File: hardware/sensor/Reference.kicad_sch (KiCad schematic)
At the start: 3 parts

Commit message: commit to save work from misbehaving laptop
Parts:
- removed R4: R, symbol Device:R
- added C?: 10u, symbol Device:C
- added Q? (x2): BC847BDW1, Package_TO_SOT_SMD:SOT-363_SC-70-6, symbol Transistor_BJT:BC847BDW1
- added U?: LTC2064, Package_SO:MSOP-8_3x3mm_P0.65mm, symbol sensorModules:LTC2064IMS8
- C13: value C -> 100n
- R3: value R -> 10k
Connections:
- net GND: now also C?.2, Q?.4 (E2)
- net V_{Ref}: now also U?.1, U?.2 (-); no longer C13.1, R3.2
- new net: Q?.1 (E1), Q?.3 (C2), Q?.5 (B2)
- new net: C13.1, C?.1, Q?.2 (B1), Q?.6 (C1), R3.2, U?.3 (+)
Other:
- moved on the sheet: C13, R3

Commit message: Fix incorrect upstream
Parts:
- removed Q? (x2): BC847BDW1, Package_TO_SOT_SMD:SOT-363_SC-70-6, symbol Transistor_BJT:BC847BDW1
- removed R3: 10k, symbol Device:R
- added J302: U_{ref}, testpoint_519x:Testpoint_519xTR, symbol Connector:Conn_01x01_Pin
- added J502: GND, testpoint_519x:Testpoint_519xTR, symbol Connector:Conn_01x01_Pin
- added R301, R302: R, Resistor_SMD:R_0805_2012Metric_Pad1.20x1.40mm_HandSolder, symbol Device:R
- C301: renamed from C13; footprint (none) -> Capacitor_SMD:C_0805_2012Metric_Pad1.18x1.45mm_HandSolder
- C302: renamed from C?; footprint (none) -> Capacitor_SMD:C_0805_2012Metric_Pad1.18x1.45mm_HandSolder
- gave numbers to parts that had none: 1
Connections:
- net GND: now also J502.1 (Pin_1), R302.2
- net V_{DD}: now also R301.1
- net at C301.1, C302.1, U301.3 (+): now also J302.1 (Pin_1), R301.2, R302.1
- net V_{Ref} renamed V_{ref}
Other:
- moved on the sheet: C301, C302

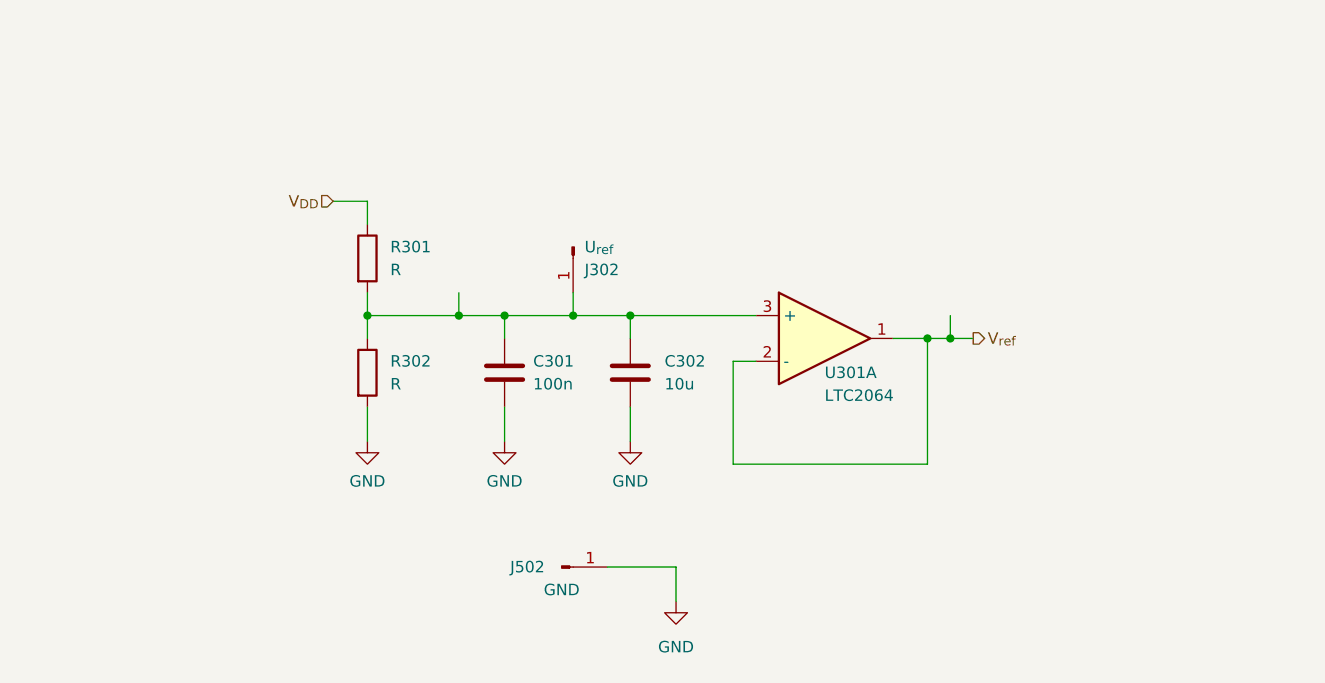
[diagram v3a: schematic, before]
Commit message: Finished initial pcb routing
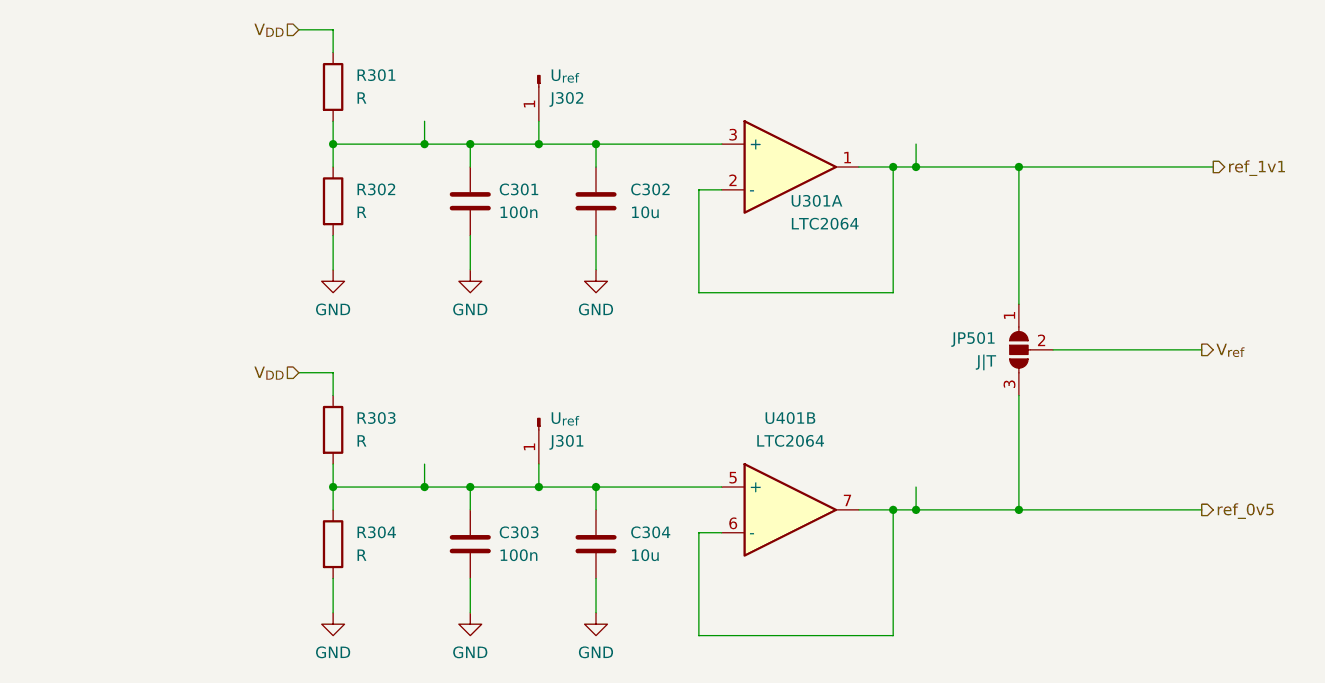
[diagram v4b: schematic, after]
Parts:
- removed J502: GND, testpoint_519x:Testpoint_519xTR, symbol Connector:Conn_01x01_Pin
- added C303: 100n, Capacitor_SMD:C_0805_2012Metric_Pad1.18x1.45mm_HandSolder, symbol Device:C
- added C304: 10u, Capacitor_SMD:C_0805_2012Metric_Pad1.18x1.45mm_HandSolder, symbol Device:C
- added J301: U_{ref}, testpoint_519x:Testpoint_519xTR, symbol Connector:Conn_01x01_Pin
- added JP501: J|T, Jumper:SolderJumper-3_P1.3mm_Open_RoundedPad1.0x1.5mm, symbol Jumper:SolderJumper_3_Open
- added R303, R304: R, Resistor_SMD:R_0805_2012Metric_Pad1.20x1.40mm_HandSolder, symbol Device:R
- added U401: LTC2064, Package_SO:MSOP-8_3x3mm_P0.65mm, symbol sensorModules:LTC2064IMS8
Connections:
- net GND: now also C303.2, C304.2, R304.2
- net V_{DD}: now also R303.1
- net V_{ref}: now also JP501.2 (C); no longer U301.1, U301.2 (-)
- new net: C303.1, C304.1, J301.1 (Pin_1), R303.2, R304.1, U401.5 (+)
- new net ref_0v5: JP501.3 (B), U401.6 (-), U401.7
- new net ref_1v1: JP501.1 (A), U301.1, U301.2 (-)
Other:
- moved on the sheet: C301, C302, J302, R301, R302, U301A

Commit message: Add bom and final version of rev 1.0
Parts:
- U301, U401: Digikey (none) -> 505-LTC2064IMS8#PBF-ND
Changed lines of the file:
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@@
+      (effects (font (size 1.27 1.27)) hide)
+    )
+    (property "Digikey" "" (at 63.5 31.75 0)
       (effects (font (size 1.27 1.27)) hide)
     )
@@
     )
     (property "Farnell" "4021217" (at 113.03 78.74 0)
+      (effects (font (size 1.27 1.27)) hide)
+    )
+    (property "Digikey" "505-LTC2064IMS8#PBF-ND" (at 113.03 78.74 0)
       (effects (font (size 1.27 1.27)) hide)
     )
@@
       (effects (font (size 1.27 1.27)) hide)
     )
+    (property "Digikey" "" (at 86.36 68.58 0)
+      (effects (font (size 1.27 1.27)) hide)
+    )
     (pin "1")
     (instances
@@
       (effects (font (size 1.27 1.27)) hide)
     )
+    (property "Digikey" "" (at 92.71 44.45 0)
+      (effects (font (size 1.27 1.27)) hide)
+    )
     (pin "1")
     (pin "2")
@@
     )
     (property "Datasheet" "~" (at 78.74 82.55 0)
+      (effects (font (size 1.27 1.27)) hide)
+    )
+    (property "Digikey" "" (at 78.74 82.55 0)
       (effects (font (size 1.27 1.27)) hide)
     )
@@
     )
     (property "Farnell" "4021217" (at 113.03 40.64 0)
+      (effects (font (size 1.27 1.27)) hide)
+    )
+    (property "Digikey" "505-LTC2064IMS8#PBF-ND" (at 113.03 40.64 0)
       (effects (font (size 1.27 1.27)) hide)
     )
@@
       (effects (font (size 1.27 1.27)) hide)
     )
+    (property "Digikey" "" (at 92.71 82.55 0)
+      (effects (font (size 1.27 1.27)) hide)
+    )
     (pin "1")
     (pin "2")
@@
       (effects (font (size 1.27 1.27)) hide)
     )
+    (property "Digikey" "" (at 63.5 44.45 0)
+      (effects (font (size 1.27 1.27)) hide)
+    )
     (pin "2")
     (pin "1")
@@
       (effects (font (size 1.27 1.27)) hide)
     )
+    (property "Digikey" "" (at 63.5 69.85 0)
+      (effects (font (size 1.27 1.27)) hide)
+    )
     (pin "2")
     (pin "1")
@@
       (effects (font (size 1.27 1.27)) hide)
     )
+    (property "Digikey" "" (at 63.5 82.55 0)
+      (effects (font (size 1.27 1.27)) hide)
+    )
     (pin "2")
     (pin "1")
@@
     )
     (property "Datasheet" "~" (at 78.74 44.45 0)
+      (effects (font (size 1.27 1.27)) hide)
+    )
+    (property "Digikey" "" (at 78.74 44.45 0)
       (effects (font (size 1.27 1.27)) hide)
     )
@@
       (effects (font (size 1.27 1.27)) hide)
     )
+    (property "Digikey" "~" (at 139.7 60.96 0)
+      (effects (font (size 1.27 1.27)) hide)
+    )
+    (property "Farnell" "~" (at 139.7 60.96 0)
+      (effects (font (size 1.27 1.27)) hide)
+    )
     (pin "3")
     (pin "2")
@@
       (effects (font (size 1.27 1.27)) hide)
     )
+    (property "Digikey" "" (at 86.36 30.48 0)
+      (effects (font (size 1.27 1.27)) hide)
+    )
